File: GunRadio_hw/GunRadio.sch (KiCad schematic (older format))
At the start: 92 parts, among them M1 MOTOR_NO_CONTACTS, Q2 LED_RGB_WS2812B, Q5 TSOP4856, Q6 TSOP4856, Q7 TSOP4856, Q8 IRLML9303, SW1 SS-1P2T, SW2 BUTTON

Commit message: - everything exept radio and processor + 7-pin connector
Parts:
- removed B1: LP603449, Installation:EEMB603030, symbol BAT
- removed C1, C2: 10n, Capacitors:CAP_0603, symbol C
- removed C13: 1000u 6v3, Capacitors:CAP_08xxR, symbol CP
- removed C20, C26, C27, C28, C32: 0.1u, Capacitors:CAP_0603, symbol C
- removed C21, C3, C4: 4.7u, Capacitors:CAP_0603, symbol C
- removed C25: 18pF, Capacitors:CAP_0603, symbol C
- removed C29, C31: 10u, Capacitors:CAP_0805, symbol C
- removed D1: SS14, Diodes:SMA_DO214AC, symbol D_Shottky
- removed D2: TSAL6200, LEDs:LED_Through-Hole-5mm, symbol LED
- removed D3: BAT54WS, Diodes:SOD323, symbol D_Shottky
- removed DA1: MCP73832, SOT:SOT23-5, symbol MCP73832
- removed DA2: NCP1529DFN, QFN_DFN:DFN6, symbol NCP1529DFN
- removed L1, L2: BLM15AG102SN1, Inductors:IND_0402, symbol L
- removed L3: 2.2uH, Inductors:IND_1515, symbol L
- removed M1: MOTOR_NO_CONTACTS, Installation:Motor_no_Contacts, symbol MOTOR_NO_CONTACTS
- removed Q2: LED_RGB_WS2812B, LEDs:LED_WS2812B, symbol LED_RGB_WS2812B
- removed Q5, Q6, Q7: TSOP4856, Sensors:TSOP48xx, symbol TSOP48xx
- removed Q8: IRLML9303, SOT:SOT23-3, symbol IRLML6302
- removed R1: 1M, Resistors:RES_0603, symbol R
- removed R10, R12, R5, R6, R7: 10k, Resistors:RES_0603, symbol R
- removed R11, R13, R23: 1k, Resistors:RES_0603, symbol R
- removed R15: 390k, Resistors:RES_0603, symbol R
- removed R16, R22: 100k, Resistors:RES_0603, symbol R
- removed R18, R19, R20: 100R, Resistors:RES_0603, symbol R
- removed R8: 4k7, Resistors:RES_0603, symbol R
- removed SW1: SS-1P2T, BtnsSwitches:SW_SS-1P2T, symbol SWITCH
- removed SW2: BUTTON, BtnsSwitches:BTN_6x6, symbol BUTTON
- removed TP1, TP2, TP3: TESTPOINT, PCB:TESTPOINT_1MM, symbol TESTPOINT-RESCUE-Head
- removed XL13: CONN_3, Connectors:PLS-3, symbol CONN_3
- removed XL14: CONN_2, Connectors:PLS-2, symbol CONN_2
- removed XL8: USB_Micro_B, Connectors:USBmicro_MOLEX_WM17142, symbol USB_MINI_B
- removed XL? (x2): RJ11, Connectors:RJ11_TJ6_6P6C, symbol RJ11
- added D?: LED, symbol LED
- added R?: 100R, Resistors:RES_0603, symbol R
- added TP? (x3): TESTPOINT, PCB:TESTPOINT_1MM, symbol TESTPOINT
- added XL?: CONN_7, symbol CONN_7
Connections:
- net labels removed: +BATT, BAT_DIRECT, Charge, D+, D-, IR_LED, IR_LED_OUT, LED_DIN, LED_DOUT, Lout, OUTER_PWR_CTRL, PwrCtrled, PwrUnst, SHLD, SNS, VCC, Vibro, VibroOut
- wire segments 270 -> 132
- no-connect marks 15 -> 17
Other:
- note added: "Power connector"
- note added: "UART"
- note removed: "5v OR Battery\nauto switch"
- note removed: "Battery"
- note removed: "Battery\nMeasurement"
- note removed: "Connector for\nouter receptacle"
- note removed: "Control of power output"
- note removed: "Crystal required for \nexact IR timings and freqs\nand USB"
- note removed: "Debug port"
- note removed: "IR Input"
- note removed: "IR LED"
- note removed: "Li-Ion charger\n2k => 0.5 A"
- note removed: "Periphery\n\nPA0: WKUP\nDAC1: IR LED\nT2: OS ticker\nT6: IR LED Chunk\nT7: IR LED Carrier\nT3C4: IR_In\nT10C1: Vibro\nSPI1: CC\nSPI2: LEDs\nUART1: UART\n\nDMA1: ADC\nDMA2: DAC\nDMA3: T3C4 IR IN\nDMA4: UART_TX\nDMA5: SPI2_TX\nDMA6: I2C1_TX\nDMA7: I2C1_RX"
- note removed: "Power +3V0"
- note removed: "RGB LED"
- note removed: "Sensors connectors"
- note removed: "Vibro"
- note removed: "uUSB \nconnector"

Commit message: scematic nearly complited
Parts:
- added C1: 1u, Capacitors:CAP_0603, symbol C
- added C2: 0.1u, Capacitors:CAP_0603, symbol C
- added DA1: NCP583SQ, SOT:SC82AB, symbol NCP583SQ
- gave numbers to parts that had none: 7
- renumbered C14 to C13, C15 to C14, C16 to C15, C17 to C16, C22 to C17, C23 to C18, C24 to C19, C30 to C20, C33 to C21, C18 to C3, C19 to C4, L4 to L1, R9 to R2, R14 to R3, R17 to R4, XL15 to XL2, XL5 to XL4, XL6 to XL5
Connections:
- net +3.3V: now also C2.1, DA1.3 (Vout)
- net +5V: now also C1.1, DA1.1 (EN), DA1.4 (Vin)
- net GND: now also C1.2, C2.2, DA1.2 (GND)
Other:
- moved on the sheet: ANT1, BLN1, C10, C11, C12, C13, C14, C15, C16, C17, C18, C19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

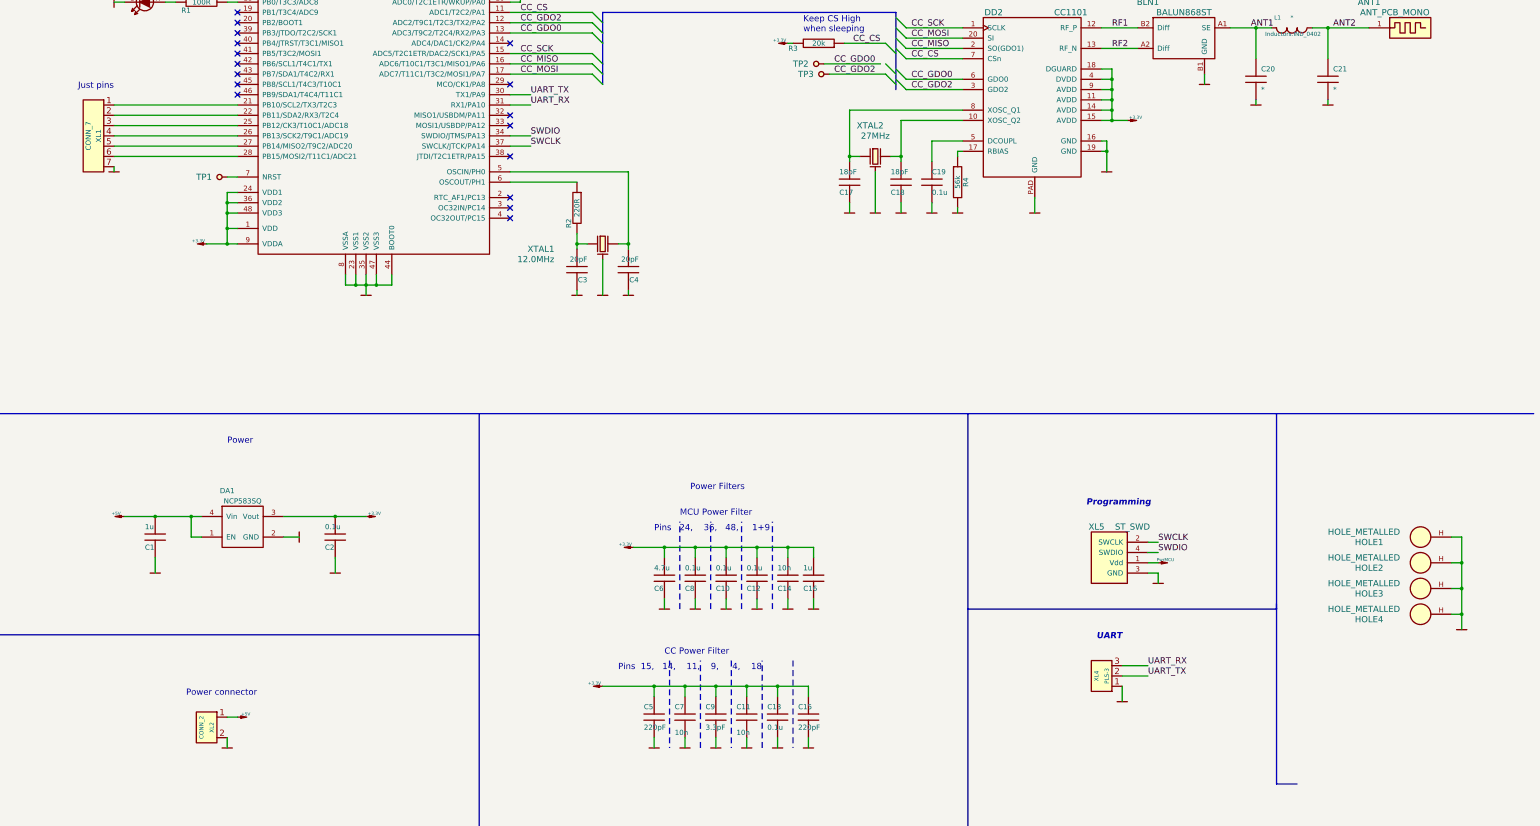
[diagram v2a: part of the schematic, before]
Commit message: GunRadioPCB started
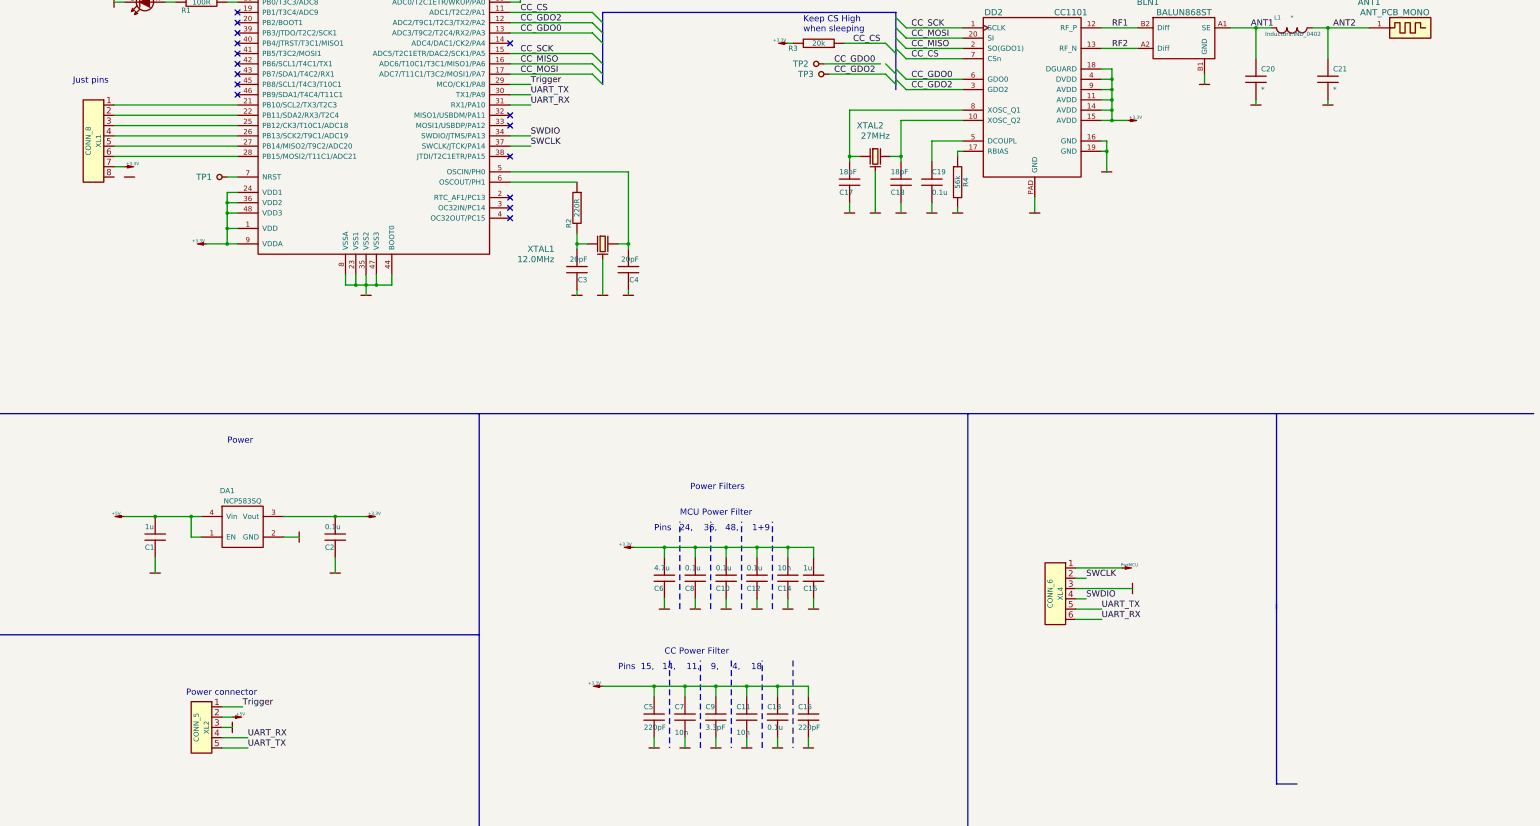
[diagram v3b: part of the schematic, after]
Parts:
- removed HOLE1, HOLE2, HOLE3, HOLE4: HOLE_METALLED, PCB:Hole3_5_out6mm, symbol HOLE_METALLED
- removed XL1: CONN_7, symbol CONN_7
- removed XL2: CONN_2, symbol CONN_2
- removed XL4: PLS-3, Connectors:PLS-3, symbol CONN_3
- removed XL5: ST_SWD, Connectors:PLS-4, symbol ST_SWD
- added XL1: CONN_8, Connectors:PLS-8, symbol CONN_8
- added XL2: CONN_5, Connectors:PLS-5, symbol CONN_5
- added XL4: CONN_6, Connectors:PLS-6, symbol CONN_6
- D1: footprint (none) -> LEDs:LED_0603
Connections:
- net +3.3V: now also XL1.7
- net +5V: now also XL2.2
- net GND: now also XL2.3, XL4.3
- net PwrMCU: now also XL4.1
- net SWCLK: now also XL4.2
- net SWDIO: now also XL4.4
- net UART_RX: now also XL2.4, XL4.6
- net UART_TX: now also XL2.5, XL4.5
- net at DD1.21 (PB10/SCL2/TX3/T2C3): now also XL1.1
- net at DD1.22 (PB11/SDA2/RX3/T2C4): now also XL1.2
- net at DD1.25 (PB12/CK3/T10C1/ADC18): now also XL1.3
- net at DD1.26 (PB13/SCK2/T9C1/ADC19): now also XL1.4
- net at DD1.27 (PB14/MISO2/T9C2/ADC20): now also XL1.5
- net at DD1.28 (PB15/MOSI2/T11C1/ADC21): now also XL1.6
- net Trigger: now reaches DD1.29 (MCO/CK1/PA8)
- net Trigger: now also XL2.1
- no-connect marks 17 -> 16
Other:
- note removed: "Programming"
- note removed: "UART"

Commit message: + GunRadio nears completion
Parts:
- ANT1: footprint Radio:ANT_868_MEANDER_4HOR_35mm -> Radio:ANT_868_GunRADIO
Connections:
- net PwrMCU is gone; now on net +3.3V: XL4.1
- net GND: now also XL1.8
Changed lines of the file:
@@
 F 0 "ANT1" H 14450 2850 60  0000 C CNN
 F 1 "ANT_PCB_MONO" H 14700 2750 60  0000 C CNN
-F 2 "Radio:ANT_868_MEANDER_4HOR_35mm" H 14650 2600 60  0001 C CNN
+F 2 "Radio:ANT_868_GunRADIO" H 14650 2600 60  0001 C CNN
 F 3 "" H 14650 2600 60  0000 C CNN
 F 4 "0" H 14650 2600 60  0001 C CNN "Price"
@@
 $EndComp
 $Comp
-L +3.3V #PWR025
+L +3.3V #PWR024
 U 1 1 56F54380
 P 7300 7650
-F 0 "#PWR025" H 7300 7610 30  0001 C CNN
+F 0 "#PWR024" H 7300 7610 30  0001 C CNN
 F 1 "+3.3V" H 7380 7680 30  0000 C CNN
 F 2 "" H 7300 7650 60  0000 C CNN
@@
 $EndComp
 $Comp
-L +3.3V #PWR026
+L +3.3V #PWR025
 U 1 1 56F54464
 P 7000 9000
-F 0 "#PWR026" H 7000 8960 30  0001 C CNN
+F 0 "#PWR025" H 7000 8960 30  0001 C CNN
 F 1 "+3.3V" H 7080 9030 30  0000 C CNN
 F 2 "" H 7000 9000 60  0000 C CNN
@@
 $EndComp
 $Comp
-L GND #PWR027
+L GND #PWR026
 U 1 1 56FADB3E
 P 7000 5200
-F 0 "#PWR027" H 7090 5180 30  0001 C CNN
+F 0 "#PWR026" H 7090 5180 30  0001 C CNN
 F 1 "GND" H 7000 5120 30  0001 C CNN
 F 2 "" H 7000 5200 60  0001 C CNN
@@
 $EndComp
 $Comp
-L GND #PWR028
+L GND #PWR027
 U 1 1 56FADB4B
 P 7250 5200
-F 0 "#PWR028" H 7340 5180 30  0001 C CNN
+F 0 "#PWR027" H 7340 5180 30  0001 C CNN
 F 1 "GND" H 7250 5120 30  0001 C CNN
 F 2 "" H 7250 5200 60  0001 C CNN
@@
 $EndComp
 $Comp
-L GND #PWR029
+L GND #PWR028
 U 1 1 56FADB51
 P 6750 5200
-F 0 "#PWR029" H 6840 5180 30  0001 C CNN
+F 0 "#PWR028" H 6840 5180 30  0001 C CNN
 F 1 "GND" H 6750 5120 30  0001 C CNN
 F 2 "" H 6750 5200 60  0001 C CNN
@@
 NoConn ~ 3450 2850
 $Comp
-L GND #PWR030
+L GND #PWR029
 U 1 1 5704284A
 P 3400 9400
-F 0 "#PWR030" H 3490 9380 30  0001 C CNN
+F 0 "#PWR029" H 3490 9380 30  0001 C CNN
 F 1 "GND" H 3400 9320 30  0001 C CNN
 F 2 "" H 3400 9400 60  0001 C CNN
@@
 $EndComp
 $Comp
-L +5V #PWR031
+L +5V #PWR030
 U 1 1 57042995
 P 3400 9300
-F 0 "#PWR031" H 3400 9260 30  0001 C CNN
+F 0 "#PWR030" H 3400 9260 30  0001 C CNN
 F 1 "+5V" H 3480 9330 30  0000 C CNN
 F 2 "" H 3400 9300 60  0000 C CNN
@@
 $EndComp
 $Comp
-L +3.3V #PWR032
+L +3.3V #PWR031
 U 1 1 570FD5AD
 P 3150 4700
-F 0 "#PWR032" H 3150 4660 30  0001 C CNN
+F 0 "#PWR031" H 3150 4660 30  0001 C CNN
 F 1 "+3.3V" H 3230 4730 30  0000 C CNN
 F 2 "" H 3150 4700 60  0000 C CNN
@@
 $EndComp
 $Comp
-L +3.3V #PWR033
+L +3.3V #PWR032
 U 1 1 570FDFAF
 P 7000 1850
-F 0 "#PWR033" H 7000 1810 30  0001 C CNN
+F 0 "#PWR032" H 7000 1810 30  0001 C CNN
 F 1 "+3.3V" H 7080 1880 30  0000 C CNN
 F 2 "" H 7000 1850 60  0000 C CNN
@@
 $EndComp
 $Comp
-L +3.3V #PWR034
+L +3.3V #PWR033
 U 1 1 570FE7C6
 P 8800 2750
-F 0 "#PWR034" H 8800 2710 30  0001 C CNN
+F 0 "#PWR033" H 8800 2710 30  0001 C CNN
 F 1 "+3.3V" H 8880 2780 30  0000 C CNN
 F 2 "" H 8800 2750 60  0000 C CNN
@@
 $EndComp
 $Comp
-L +3.3V #PWR035
+L +3.3V #PWR034
 U 1 1 570FECA9
 P 12100 3500
-F 0 "#PWR035" H 12100 3460 30  0001 C CNN
+F 0 "#PWR034" H 12100 3460 30  0001 C CNN
 F 1 "+3.3V" H 12180 3530 30  0000 C CNN
 F 2 "" H 12100 3500 60  0000 C CNN
@@
 $EndComp
 $Comp
-L GND #PWR036
+L GND #PWR035
 U 1 1 57103126
 P 2250 2350
-F 0 "#PWR036" H 2340 2330 30  0001 C CNN
+F 0 "#PWR035" H 2340 2330 30  0001 C CNN
 F 1 "GND" H 2250 2270 30  0001 C CNN
 F 2 "" H 2250 2350 60  0000 C CNN
@@
 $EndComp
 $Comp
-L GND #PWR037
+L GND #PWR036
 U 1 1 570EC462
 P 4050 7550
-F 0 "#PWR037" H 4140 7530 30  0001 C CNN
+F 0 "#PWR036" H 4140 7530 30  0001 C CNN
 F 1 "GND" H 4050 7470 30  0001 C CNN
 F 2 "" H 4050 7550 60  0000 C CNN
@@
 $EndComp
 $Comp
-L +3.3V #PWR038
+L +3.3V #PWR037
 U 1 1 570EC708
 P 4700 7350
-F 0 "#PWR038" H 4700 7310 30  0001 C CNN
+F 0 "#PWR037" H 4700 7310 30  0001 C CNN
 F 1 "+3.3V" H 4780 7380 30  0000 C CNN
 F 2 "" H 4700 7350 60  0000 C CNN
@@
 $EndComp
 $Comp
-L GND #PWR039
+L GND #PWR038
 U 1 1 570EC88F
 P 4400 7900
-F 0 "#PWR039" H 4490 7880 30  0001 C CNN
+F 0 "#PWR038" H 4490 7880 30  0001 C CNN
 F 1 "GND" H 4400 7820 30  0001 C CNN
 F 2 "" H 4400 7900 60  0000 C CNN
@@
 $EndComp
 $Comp
-L GND #PWR040
+L GND #PWR039
 U 1 1 570ECB72
 P 2650 7900
-F 0 "#PWR040" H 2740 7880 30  0001 C CNN
+F 0 "#PWR039" H 2740 7880 30  0001 C CNN
 F 1 "GND" H 2650 7820 30  0001 C CNN
 F 2 "" H 2650 7900 60  0000 C CNN
@@
 $EndComp
 $Comp
-L +5V #PWR041
+L +5V #PWR040
 U 1 1 570ED48A
 P 2350 7350
-F 0 "#PWR041" H 2350 7310 30  0001 C CNN
+F 0 "#PWR040" H 2350 7310 30  0001 C CNN
 F 1 "+5V" H 2430 7380 30  0000 C CNN
 F 2 "" H 2350 7350 60  0000 C CNN
@@
 $EndComp
 $Comp
-L GND #PWR042
+L GND #PWR041
 U 1 1 5714DC60
 P 12150 8050
-F 0 "#PWR042" H 12240 8030 30  0001 C CNN
+F 0 "#PWR041" H 12240 8030 30  0001 C CNN
 F 1 "GND" H 12150 7970 30  0001 C CNN
 F 2 "" H 12150 8050 60  0001 C CNN
@@
 Text Label 11850 8350 0    60   ~ 0
 UART_RX
-$Comp
-L PwrMCU #PWR043
-U 1 1 5714DC6A
-P 12050 7850
-F 0 "#PWR043" H 12050 7900 30  0001 C CNN
-F 1 "PwrMCU" H 12120 7880 30  0000 C CNN
-F 2 "" H 12050 7850 60  0000 C CNN
-F 3 "" H 12050 7850 60  0000 C CNN
-	1    12050 7850
-	1    0    0    -1
-$EndComp
 $Comp
 L CONN_6 XL4
@@
 $EndComp
 $Comp
-L +3.3V #PWR044
+L +3.3V #PWR042
 U 1 1 5714DDD0
 P 2350 3950
-F 0 "#PWR044" H 2350 3910 30  0001 C CNN
+F 0 "#PWR042" H 2350 3910 30  0001 C CNN
 F 1 "+3.3V" H 2430 3980 30  0000 C CNN
 F 2 "" H 2350 3950 60  0000 C CNN
@@
 $EndComp
 $Comp
-L GND #PWR045
+L GND #PWR043
 U 1 1 5714DF2E
 P 2400 4050
-F 0 "#PWR045" H 2490 4030 30  0001 C CNN
+F 0 "#PWR043" H 2490 4030 30  0001 C CNN
 F 1 "GND" H 2400 3970 30  0001 C CNN
 F 2 "" H 2400 4050 60  0000 C CNN
 F 3 "" H 2400 4050 60  0000 C CNN
 	1    2400 4050
-	1    0    0    -1
+	0    1    1    0
 $EndComp
 Wire Wire Line
@@
 	9750 3050 9200 3050
 Wire Wire Line
-	9150 2950 9700 2950
+	9150 2950 9750 2950
 Wire Bus Line
 	9850 2450 9850 3200
@@
 Wire Wire Line
 	3500 9200 3300 9200
+$Comp
+L +3.3V #PWR044
+U 1 1 57155D2A
+P 12050 7850
+F 0 "#PWR044" H 12050 7810 30  0001 C CNN
+F 1 "+3.3V" H 12130 7880 30  0000 C CNN
+F 2 "" H 12050 7850 60  0000 C CNN
+F 3 "" H 12050 7850 60  0000 C CNN
+	1    12050 7850
+	1    0    0    -1
+$EndComp
+Wire Wire Line
+	2400 4050 2250 4050
 $EndSCHEMATC
